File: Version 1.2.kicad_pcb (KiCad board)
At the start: 4 copper layers, 40 x 40 mm, 33 parts, among them J1 Conn_01x04_Pin, J2 Screw_Terminal_01x02, J3 Conn_01x07_Pin, J4 Conn_Coaxial, U1 BGA2801, U2 BGA420, U3 AS179-92LF, U4 SX1278, U5 74LVC1G19, Y1 ECS-TXO-2520-33-400-AN-TR

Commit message: EMI & Compression
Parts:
- J2: value Screw_Terminal_01x02 -> Conn_01x02_Pin; footprint Screw Connector 01x02:1725656 -> Connector_PinHeader_1.27mm:PinHeader_1x02_P1.27mm_Vertical
- moved J2 16.3 mm to (127.6, 71.4)
- moved J1 8.33 mm to (140.1, 71.5)
- moved R1 7.12 mm to (144.6, 80.1), turned to 0 degrees
- moved J4 6.15 mm to (154.0, 96.7)
- moved C5 3.18 mm to (142.5, 98.7)
- moved L3 3.18 mm to (142.5, 96.8)
- moved C1 2.61 mm to (133.2, 101.7)
- moved C4 2.61 mm to (138.4, 101.7)
- moved L1 2.61 mm to (135.8, 101.0)
- moved L2 2.61 mm to (140.9, 101.0)
- moved J3 2.07 mm to (153.1, 75.3)
- moved U2 2.07 mm to (136.4, 92.1)
- moved U3 2.07 mm to (133.3, 98.4)
- moved U4 2.07 mm to (137.9, 84.4)
- moved Y1 2.07 mm to (144.0, 89.8)
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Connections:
- J2 pad 1: +3.3V -> GND
- J2 pad 2: GND -> +3.3V
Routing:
- net /Reset: track 22.8 -> 29.3 mm
- net /Filter_Output: track 2.84 -> 9.20 mm
- net /NSS: track 15.2 -> 10.3 mm
- net /MOSI: track 14.7 -> 10.1 mm
- net /MISO: track 14.4 -> 10.0 mm
- net /SCK: track 14.2 -> 10.3 mm
- net GND: track 76.6 -> 72.7 mm
- net /Filter_Input: track 3.96 -> 3.31 mm
- net Net-(C5-Pad1): track 3.61 -> 4.22 mm

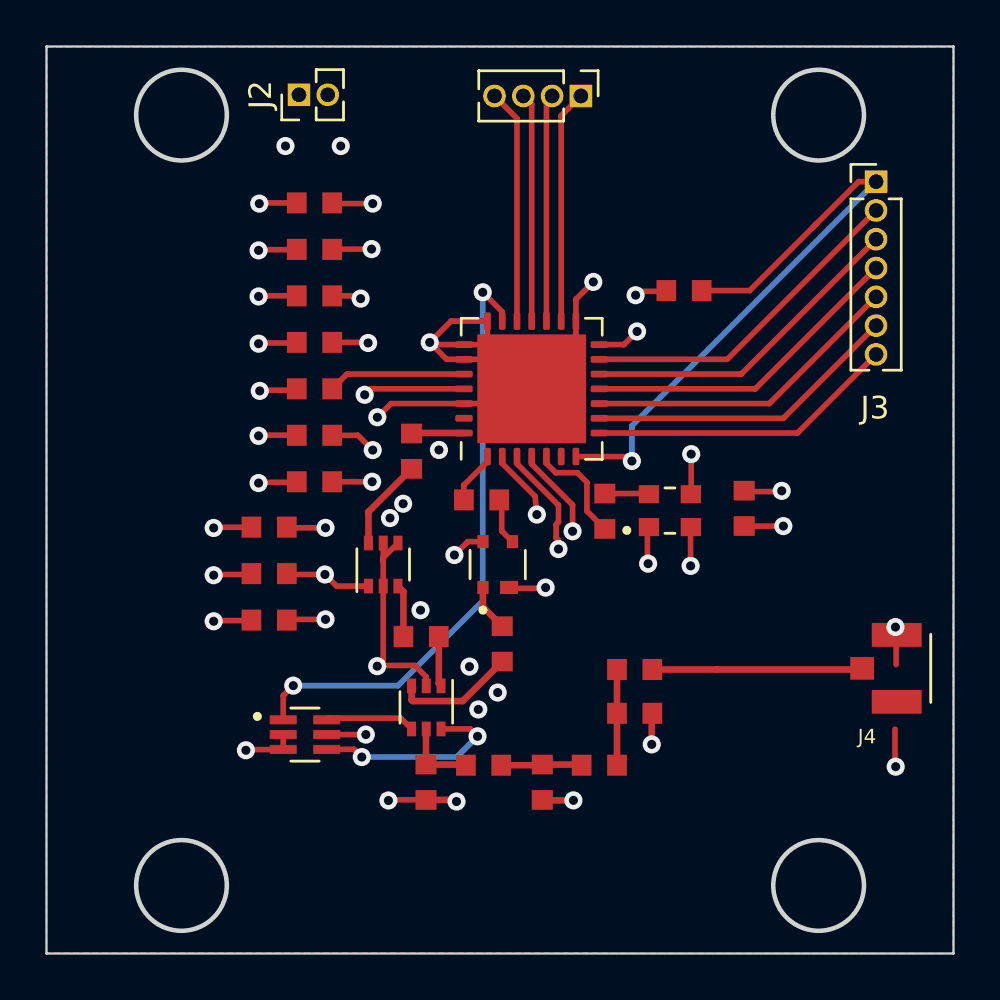
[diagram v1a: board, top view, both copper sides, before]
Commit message: Fixed signal lines In preparation for EMI Shielding.
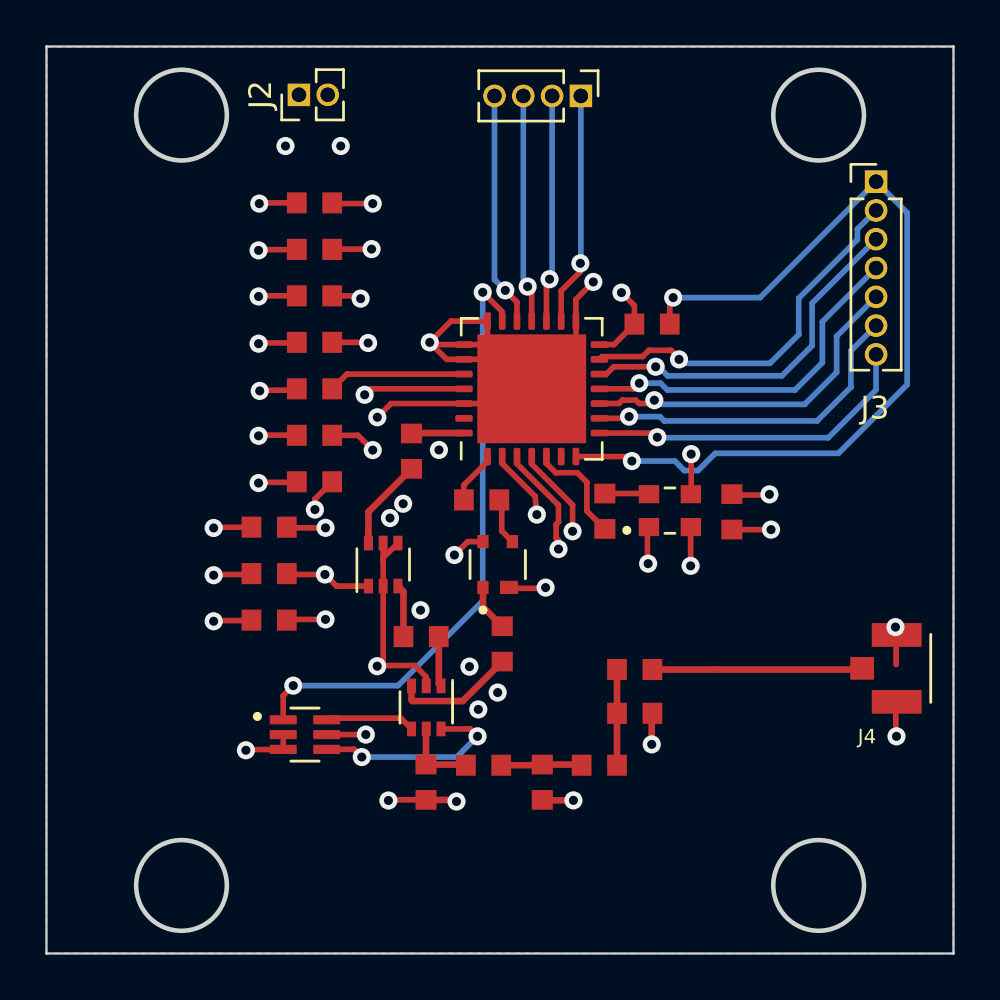
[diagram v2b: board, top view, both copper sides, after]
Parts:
- moved R1 2.04 mm to (143.2, 81.5)
- moved C6 0.57 mm to (146.7, 89.8)
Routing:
- net /Reset: track 29.3 -> 38.3 mm, vias 1 -> 2
- net Net-(U4-VR_ANA): track 15.5 -> 18.5 mm
- net Net-(U4-VR_DIG): track 19.6 -> 22.2 mm
- net /DIO_5: track 14.9 -> 16.6 mm, vias 0 -> 1
- net /DIO_4: track 14.7 -> 16.1 mm, vias 0 -> 1
- net /DIO_3: track 14.4 -> 15.7 mm, vias 0 -> 1
- net /DIO_2: track 14.2 -> 15.4 mm, vias 0 -> 1
- net /DIO_1: track 13.9 -> 15.0 mm, vias 0 -> 1
- net /DIO_0: track 13.6 -> 14.7 mm, vias 0 -> 1
- net /MISO: track 10.0 -> 10.4 mm, vias 0 -> 1
- net +3.3V: track 31.3 -> 31.2 mm, vias 15 -> 14
- net /SCK: vias 0 -> 1
- net /NSS: vias 0 -> 1
- net /MOSI: vias 0 -> 1
